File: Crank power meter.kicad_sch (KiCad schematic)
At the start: 27 parts, among them J1 Conn_02x03_Odd_Even, J4 Conn_01x04_Pin, Q1 PNP, U1 ESP32-S3-MINI-1, U2 MCP1825S, U3 HX711

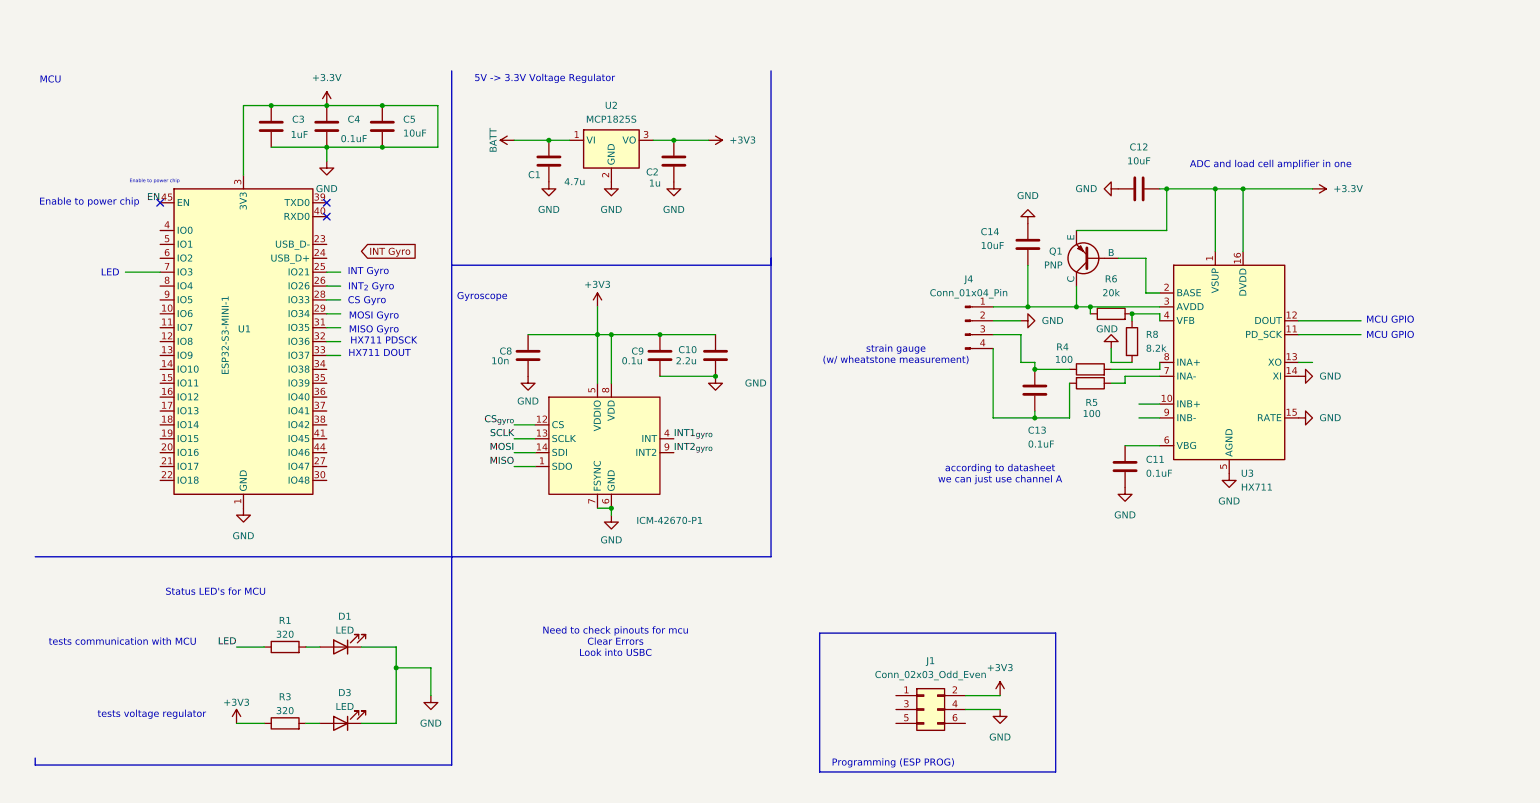
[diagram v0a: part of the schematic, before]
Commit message: Replaced text with their corresponding labels
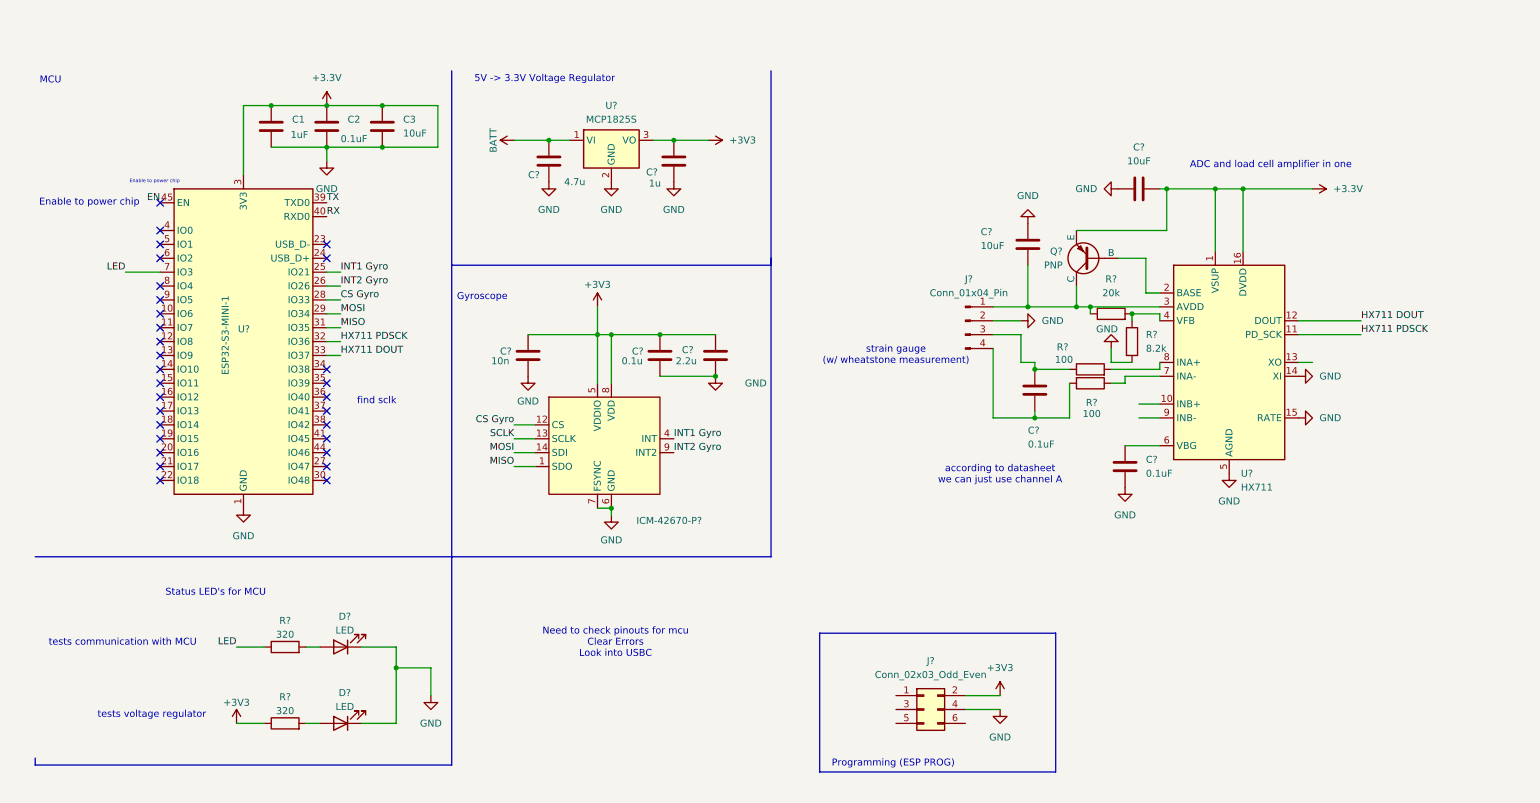
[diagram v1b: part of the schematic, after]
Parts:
- renumbered C3 to C1, C4 to C2, C5 to C3, C8 to C?, C1 to C?, C11 to C?, C12 to C?, C14 to C?, C13 to C?, C9 to C?, C10 to C?, C2 to C?, D1 to D?, D3 to D?, ICM-42670-P1 to ICM-42670-P?, J4 to J?, J1 to J?, Q1 to Q?, R5 to R?, R3 to R?, R8 to R?, R4 to R?, R6 to R?, R1 to R?, U1 to U?, U2 to U?, U3 to U?
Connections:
- net CS_{gyro} is gone; now on net CS Gyro: ICM-42670-P?.12 (CS)
- net INT1_{gyro} is gone; now on net INT1 Gyro: ICM-42670-P?.4 (INT)
- net INT2_{gyro} is gone; now on net INT2 Gyro: ICM-42670-P?.9 (INT2)
- net LED: now also U?.7 (IO3)
- net MISO: now also U?.31 (IO35)
- net MOSI: now also U?.29 (IO34)
- net INT1 Gyro: now reaches U?.25 (IO21)
- net INT2 Gyro: now reaches U?.26 (IO26)
- net CS Gyro: now reaches U?.28 (IO33)
- net HX711 PDSCK: now reaches U?.32 (IO36)
- net HX711 PDSCK: now also U?.11 (PD_SCK)
- net HX711 DOUT: now reaches U?.33 (IO37)
- net HX711 DOUT: now also U?.12 (DOUT)
- net TX: now reaches U?.39 (TXD0)
- net RX: now reaches U?.40 (RXD0)
- no-connect marks 3 -> 30
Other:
- note added: "find sclk"
- note removed: "CS Gyro"
- note removed: "HX711 DOUT"
- note removed: "HX711 PDSCK"
- note removed: "INT Gyro"
- note removed: "INT_{2} Gyro"
- note removed: "LED"
- note removed: "MCU GPIO"
- note removed: "MISO Gyro"
- note removed: "MOSI Gyro"

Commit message: Added SCLK to ESP32
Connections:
- net SCLK: now also U?.12 (IO8)
- no-connect marks 30 -> 29
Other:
- note removed: "find sclk"
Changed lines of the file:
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@@
-		)
-	)
-	(text "find sclk\n"
-		(exclude_from_sim no)
-		(at 75.184 73.152 0)
-		(effects
-			(font
-				(size 1.27 1.27)
-			)
 		)
 	)
@@
 	)
 	(no_connect
-		(at 35.56 62.23)
-	)
-	(no_connect
 		(at 66.04 44.45)
 	)
@@
 		(pts
 			(xy 76.2 26.67) (xy 86.36 26.67)
+		)
+		(stroke
+			(width 0)
+			(type default)
+		)
+	)
+	(wire
+		(pts
+			(xy 29.21 62.23) (xy 35.56 62.23)
 		)
 		(stroke
@@
 		)
 	)
+	(label "SCLK"
+		(at 100.33 80.01 180)
+		(effects
+			(font
+				(size 1.27 1.27)
+			)
+			(justify right bottom)
+		)
+	)
 	(label ""
 		(at 74.93 53.34 0)
@@
 		)
 	)
+	(label "SCLK"
+		(at 29.21 62.23 180)
+		(effects
+			(font
+				(size 1.27 1.27)
+			)
+			(justify right bottom)
+		)
+	)
 	(label "HX711 DOUT"
 		(at 255.27 58.42 0)
@@
 		)
 	)
-	(label "SCLK"
-		(at 100.33 80.01 180)
-		(effects
-			(font
-				(size 1.27 1.27)
-			)
-			(justify right bottom)
-		)
-	)
